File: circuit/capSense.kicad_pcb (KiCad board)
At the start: 2 copper layers, 27.9 x 40.6 mm, 16 parts, among them P1 Capsense, P2 PWR_IN, P3 RS 232 TTL, P4 gpio, SW1 SW_PUSH, U1 ESP-12E

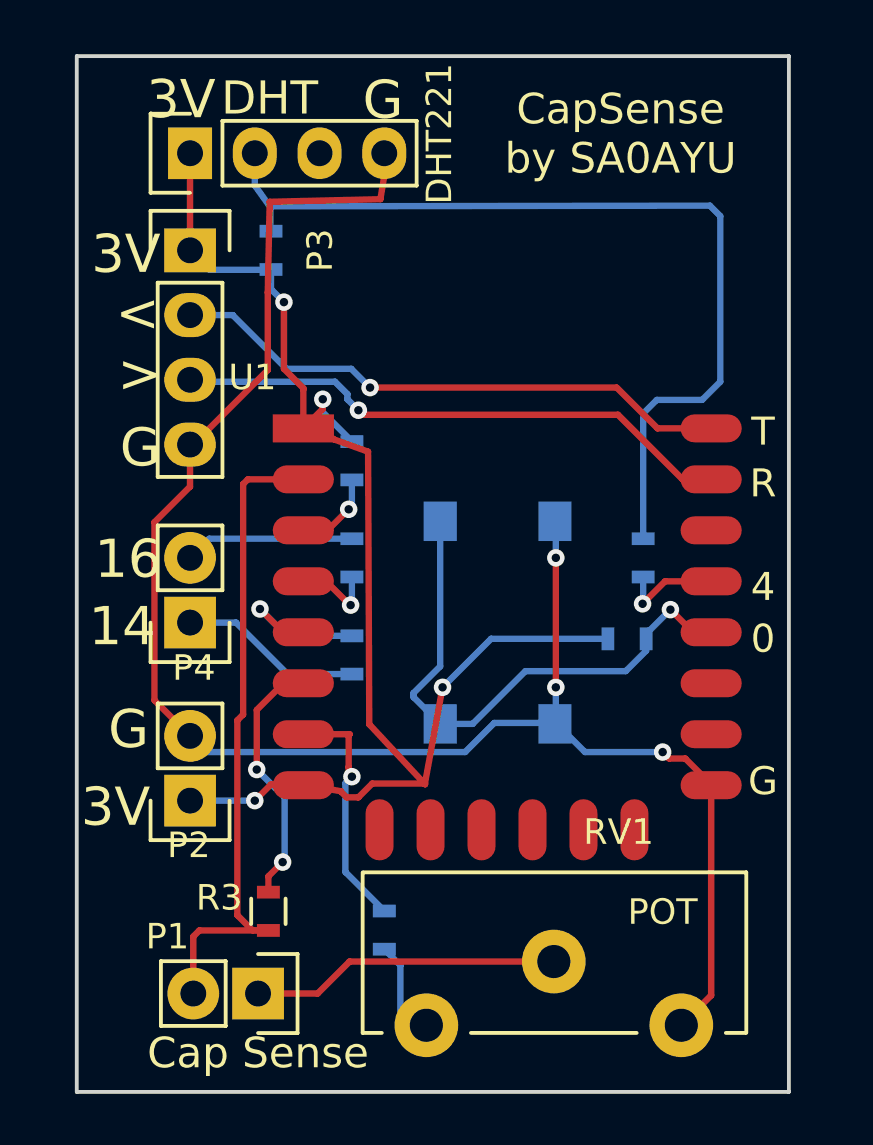
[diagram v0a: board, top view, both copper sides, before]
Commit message: new version of PCB with support for waterlog
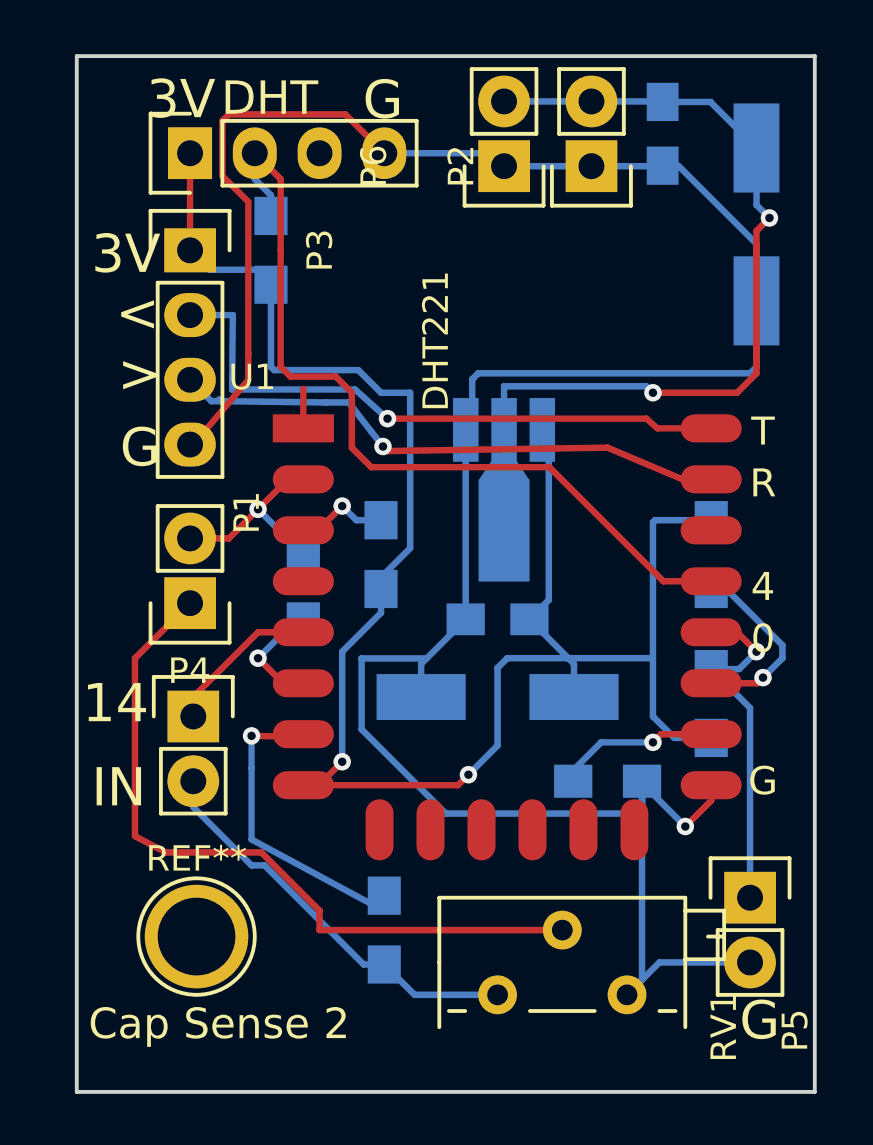
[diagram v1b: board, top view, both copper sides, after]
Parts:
- removed R4: 0, Resistors_SMD:R_0603
- removed SW1: SW_PUSH, Buttons_Switches_SMD:SW_SPST_PTS645
- added C1: 100n, Capacitors_SMD:C_0805_HandSoldering, B.Cu at (78.9, 43.1)
- added C3: 10u, Capacitors_Tantalum_SMD:TantalC_SizeC_EIA-6032_HandSoldering, B.Cu at (82.5, 46.6)
- added C4: 10u, Capacitors_Tantalum_SMD:TantalC_SizeC_EIA-6032_HandSoldering, B.Cu at (72.4, 65.2)
- added C5: 100n, Capacitors_SMD:C_0805_HandSoldering, B.Cu at (72.4, 62.1)
- added P5: flash, Socket_Strips:Socket_Strip_Straight_1x02, F.Cu at (82.3, 73.0)
- added P6: 5V_IN, Socket_Strips:Socket_Strip_Straight_1x02, F.Cu at (72.6, 44.3)
- added REF**: 1pin, Connect:1pin, F.Cu at (60.6, 74.5)
- added U2: HT7333-A, TO_SOT_Packages_SMD:SOT89-3_Housing_Handsoldering, B.Cu at (72.6, 57.0)
- P2: value PWR_IN -> 5V_IN
- R1, R2, R5, R8: footprint Resistors_SMD:R_0603 -> Resistors_SMD:R_0805_HandSoldering
- R3: footprint Resistors_SMD:R_0603 -> Resistors_SMD:R_0805_HandSoldering; moved to B.Cu
- R6, R7: value 0 -> 4.7k; footprint Resistors_SMD:R_0603 -> Resistors_SMD:R_0805_HandSoldering
- RV1: footprint Potentiometers:Potentiometer_Trimmer-Piher-PT15-h2-5_vertical -> Potentiometers:Potentiometer_Bourns_3296Z_3-8Zoll_Angular_ScrewFront
- moved P2 29.5 mm to (76.1, 44.3)
- moved P1 15.5 mm to (60.3, 61.5), turned to 90 degrees
- moved R6 13.3 mm to (76.7, 68.5), turned to 0 degrees
- moved R3 12.8 mm to (64.8, 60.8), turned to 90 degrees
- moved R8 4.17 mm to (80.8, 65.4), turned to 90 degrees
- moved R1 3.86 mm to (67.8, 59.6), turned to 270 degrees
- moved P4 3.69 mm to (60.5, 65.9), turned to 270 degrees
- moved RV1 3.04 mm to (72.4, 76.8), turned to 270 degrees
- moved R7 2.67 mm to (80.8, 59.6)
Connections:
- P2 pad 1: +3V3 -> GND
- P2 pad 2: GND -> +5V
- R5 pad 2: Net-(R5-Pad2) -> Net-(P4-Pad2)
- R6 pad 2: Net-(P4-Pad2) -> GND
- R7 pad 1: Net-(DHT221-Pad2) -> +3V3
- RV1 pad 1: Net-(R5-Pad2) -> Net-(P4-Pad2)
- U1 pad 1: +3V3 -> Net-(U1-Pad1)
- U1 pad 16: Net-(U1-Pad16) -> Net-(R6-Pad1)
- U1 pad 17: Net-(U1-Pad17) -> Net-(R7-Pad2)
- U1 pad 19: Net-(R7-Pad2) -> Net-(DHT221-Pad2)
- U1 pad 4: Net-(R6-Pad1) -> Net-(U1-Pad1)
- U1 pad 5: Net-(R4-Pad1) -> Net-(P4-Pad1)
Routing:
- net GND: track 69.8 -> 103.6 mm, vias 3 -> 1
- net +5V: track 0.00 -> 32.0 mm, vias 0 -> 2
- net +3V3: track 55.4 -> 77.0 mm, vias 4 -> 2
- net Net-(P1-Pad2): track 26.2 -> 7.89 mm, vias 0 -> 1
- net Net-(P1-Pad1): track 12.1 -> 28.7 mm
- net Net-(P4-Pad2): track 6.66 -> 16.0 mm
- net Net-(P5-Pad1): track 22.1 -> 14.5 mm
- net Net-(R4-Pad1): track 6.12 -> 0.00 mm, vias 1 -> 0
- net Net-(R3-Pad1): track 10.1 -> 5.34 mm, vias 2 -> 1
- net Net-(R5-Pad2): track 3.32 -> 0.00 mm
- net Net-(R7-Pad2): track 4.12 -> 7.42 mm
- net Net-(R6-Pad1): track 3.37 -> 6.43 mm
- net Net-(U1-Pad1): track 0.00 -> 2.95 mm
- net Net-(R5-Pad1): track 9.58 -> 12.5 mm
- net Net-(DHT221-Pad2): track 36.1 -> 34.2 mm
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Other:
- board size 27.9 x 40.6 mm -> 29 x 40.6 mm
- board text added: "Cap Sense 2"
- board text added: "CapSense 2 by SA0AYU"
- board text added: "IN"
- board text added: "vcc"
- board text removed: "16"
- board text removed: "Cap Sense"
- board text removed: "CapSense by SA0AYU"
